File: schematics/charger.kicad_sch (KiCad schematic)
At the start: 22 parts, among them J1 USB_C_Receptacle_USB2.0_14P, U1 IP2326

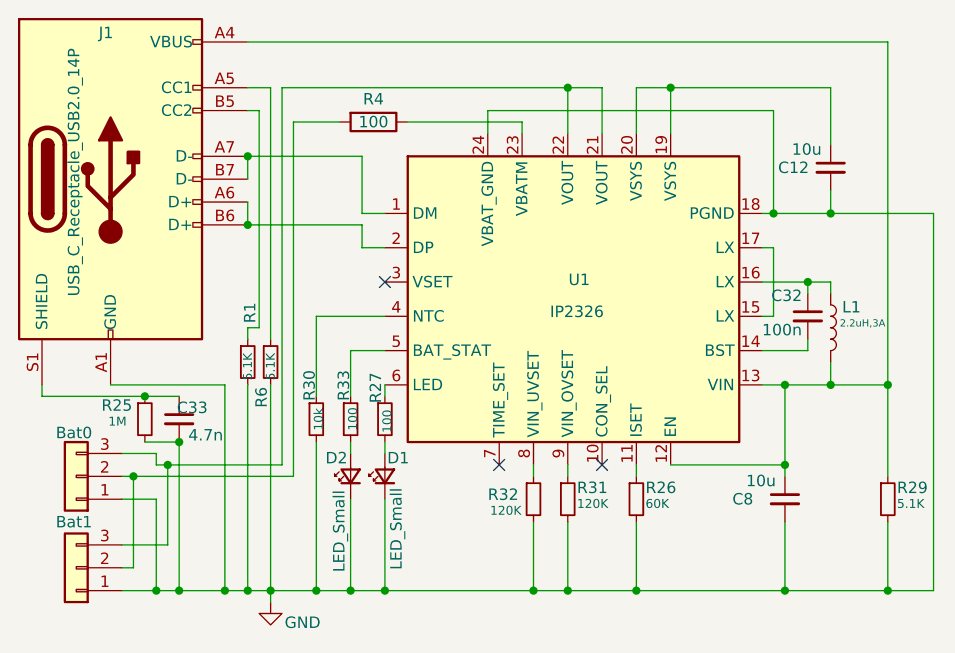
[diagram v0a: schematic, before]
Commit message: add power to the rest
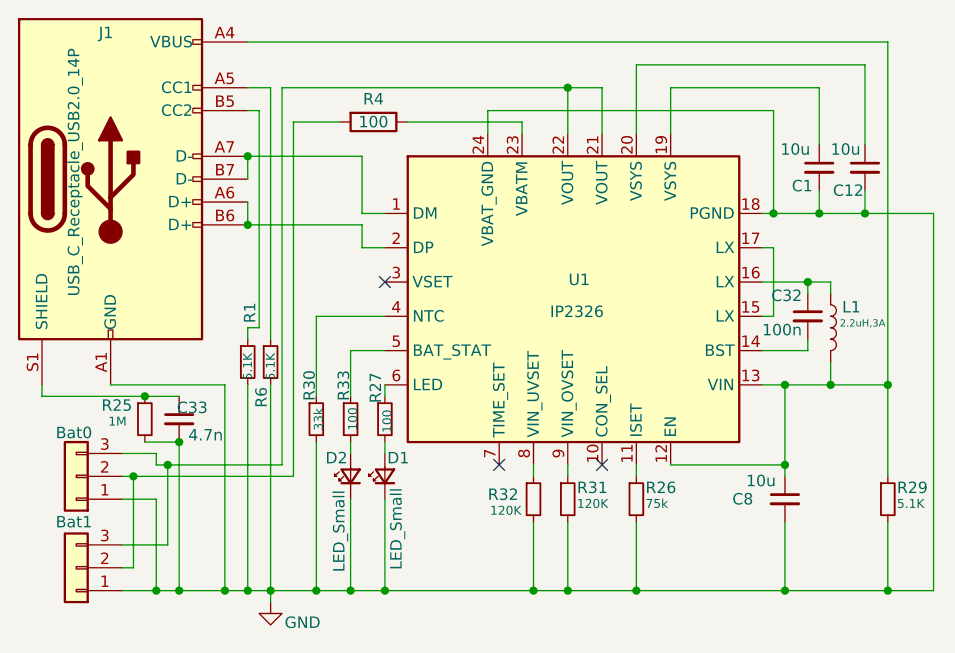
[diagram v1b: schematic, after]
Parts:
- added C1: 10u, Capacitor_SMD:C_0603_1608Metric, symbol uRX:C_Small
- R26: value 60K -> 75k
- R30: value 10k -> 33k
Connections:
- net GND: now also C1.2
- net at C12.1, U1.20 (VSYS): no longer U1.19 (VSYS)
- new net: C1.1, U1.19 (VSYS)
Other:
- moved on the sheet: C12
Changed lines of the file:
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@@
+	)
+	(junction
+		(at 187.96 77.47)
+		(diameter 0)
+		(color 0 0 0 0)
 	)
 	(junction
@@
 	)
 	(junction
-		(at 189.23 77.47)
-		(diameter 0)
-		(color 0 0 0 0)
-	)
-	(junction
 		(at 195.58 96.52)
 		(diameter 0)
@@
 	)
 	(junction
-		(at 171.45 63.5)
+		(at 193.04 77.47)
 		(diameter 0)
 		(color 0 0 0 0)
@@
 	(wire
 		(pts
+			(xy 193.04 77.47) (xy 200.66 77.47)
+		)
+		(stroke
+			(width 0)
+			(type default)
+		)
+	)
+	(wire
+		(pts
 			(xy 135.89 97.79) (xy 135.89 92.71)
 		)
@@
 	(wire
 		(pts
-			(xy 171.45 63.5) (xy 171.45 68.58)
-		)
-		(stroke
-			(width 0)
-			(type default)
-		)
-	)
-	(wire
-		(pts
 			(xy 163.83 68.58) (xy 163.83 63.5)
 		)
@@
 	(wire
 		(pts
-			(xy 189.23 77.47) (xy 200.66 77.47)
-		)
-		(stroke
-			(width 0)
-			(type default)
-		)
-	)
-	(wire
-		(pts
 			(xy 137.16 81.28) (xy 139.7 81.28)
 		)
@@
 	(wire
 		(pts
-			(xy 182.88 77.47) (xy 189.23 77.47)
+			(xy 182.88 77.47) (xy 187.96 77.47)
 		)
 		(stroke
@@
 	(wire
 		(pts
+			(xy 171.45 63.5) (xy 187.96 63.5)
+		)
+		(stroke
+			(width 0)
+			(type default)
+		)
+	)
+	(wire
+		(pts
 			(xy 121.92 96.52) (xy 121.92 119.38)
 		)
@@
 	(wire
 		(pts
-			(xy 189.23 74.93) (xy 189.23 77.47)
+			(xy 193.04 74.93) (xy 193.04 77.47)
 		)
 		(stroke
@@
 	(wire
 		(pts
+			(xy 187.96 74.93) (xy 187.96 77.47)
+		)
+		(stroke
+			(width 0)
+			(type default)
+		)
+	)
+	(wire
+		(pts
 			(xy 115.57 105.41) (xy 128.27 105.41)
 		)
@@
 	(wire
 		(pts
+			(xy 187.96 77.47) (xy 193.04 77.47)
+		)
+		(stroke
+			(width 0)
+			(type default)
+		)
+	)
+	(wire
+		(pts
 			(xy 110.49 106.68) (xy 111.76 106.68)
 		)
@@
 	(wire
 		(pts
-			(xy 189.23 69.85) (xy 189.23 63.5)
+			(xy 193.04 69.85) (xy 193.04 60.96)
 		)
 		(stroke
@@
 	(wire
 		(pts
+			(xy 187.96 63.5) (xy 187.96 69.85)
+		)
+		(stroke
+			(width 0)
+			(type default)
+		)
+	)
+	(wire
+		(pts
 			(xy 139.7 109.22) (xy 139.7 119.38)
 		)
@@
 	(wire
 		(pts
-			(xy 189.23 63.5) (xy 171.45 63.5)
+			(xy 167.64 60.96) (xy 193.04 60.96)
 		)
 		(stroke
@@
 	(wire
 		(pts
+			(xy 171.45 68.58) (xy 171.45 63.5)
+		)
+		(stroke
+			(width 0)
+			(type default)
+		)
+	)
+	(wire
+		(pts
 			(xy 135.89 92.71) (xy 139.7 92.71)
 		)
@@
 	(wire
 		(pts
-			(xy 167.64 63.5) (xy 167.64 68.58)
+			(xy 167.64 60.96) (xy 167.64 68.58)
 		)
 		(stroke
@@
 		(pts
 			(xy 124.46 71.12) (xy 137.16 71.12)
-		)
-		(stroke
-			(width 0)
-			(type default)
-		)
-	)
-	(wire
-		(pts
-			(xy 171.45 63.5) (xy 167.64 63.5)
 		)
 		(stroke
@@
 			)
 		)
-		(property "Value" "60K"
+		(property "Value" "75k"
 			(at 168.656 109.728 0)
 			(effects
@@
 	(symbol
 		(lib_id "uRX:C_Small")
-		(at 189.23 72.39 0)
+		(at 193.04 72.39 0)
 		(unit 1)
 		(exclude_from_sim no)
@@
 		(dnp no)
 		(property "Reference" "C12"
-			(at 183.388 72.39 0)
+			(at 189.484 74.93 0)
 			(effects
 				(font
@@
 		)
 		(property "Value" "10u"
-			(at 184.912 70.358 0)
+			(at 189.23 70.358 0)
 			(effects
 				(font
@@
 		)
 		(property "Footprint" "Capacitor_SMD:C_0603_1608Metric"
-			(at 189.23 72.39 0)
+			(at 193.04 72.39 0)
 			(effects
 				(font
@@
 		)
 		(property "Datasheet" "~"
-			(at 189.23 72.39 0)
+			(at 193.04 72.39 0)
 			(effects
 				(font
@@
 		)
 		(property "Description" ""
-			(at 189.23 72.39 0)
+			(at 193.04 72.39 0)
 			(effects
 				(font
@@
 				(path "/622e7602-97f9-4d02-97fb-abddf1d4012c"
 					(reference "C12")
+					(unit 1)
+				)
+			)
+		)
+	)
+	(symbol
+		(lib_id "uRX:C_Small")
+		(at 187.96 72.39 0)
+		(unit 1)
+		(exclude_from_sim no)
+		(in_bom yes)
+		(on_board yes)
+		(dnp no)
+		(property "Reference" "C1"
+			(at 184.912 74.422 0)
+			(effects
+				(font
+					(size 1.27 1.27)
+				)
+				(justify left)
+			)
+		)
+		(property "Value" "10u"
+			(at 183.642 70.358 0)
+			(effects
+				(font
+					(size 1.27 1.27)
+				)
+				(justify left)
+			)
+		)
+		(property "Footprint" "Capacitor_SMD:C_0603_1608Metric"
+			(at 187.96 72.39 0)
+			(effects
+				(font
+					(size 1.27 1.27)
+				)
+				(hide yes)
+			)
+		)
+		(property "Datasheet" "~"
+			(at 187.96 72.39 0)
+			(effects
+				(font
+					(size 1.27 1.27)
+				)
+				(hide yes)
+			)
+		)
+		(property "Description" ""
+			(at 187.96 72.39 0)
+			(effects
+				(font
+					(size 1.27 1.27)
+				)
+			)
+		)
+		(pin "1"
+		)
+		(pin "2"
+		)
+		(instances
+			(project "charger"
+				(path "/622e7602-97f9-4d02-97fb-abddf1d4012c"
+					(reference "C1")
 					(unit 1)
 				)
@@
 			)
 		)
-		(property "Value" "10k"
+		(property "Value" "33k"
 			(at 132.334 101.6 90)
 			(effects
